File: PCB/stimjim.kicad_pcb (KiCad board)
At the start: 4 copper layers, 129 x 79.5 mm, 224 parts, among them J1 302-R161, J10 USB4105-GF-A, J11 BM03B-SRSS-TB, J2 0731375003, J3 0731375003, J4 10129383-910002ALF, J7 0731375003, J9 0731375003, SW2 PTS645VH58-2 LFS, SW3 TS04-66-50-BK-160-SMT, U1 OPA197, U10 AMP03, U11 INA826, U12 DG409DYZ-T, U13 CC3-0512DF-E, U14 ISO7760, U15 ISO7741, U151 AP2112K-3.3, U16 MC78L05ACDR2G, U17 AD5752, U18 AD7321, U19 AD1582, U2 CC3-0512DF-E, U20 OPA197, U21 AMP03, U22 INA826, U23 DG409DYZ-T, U24 RP2354B, U25 W25Q128JVS, U26 OPA197, U3 ISO7760, U4 ISO7741, U5 MC78L05ACDR2G, U6 AD5752, U7 AD7321, U8 AD1582, U9 OPA197, Y1 ABM8AIG-12.000MHZ-12-2Z-T3

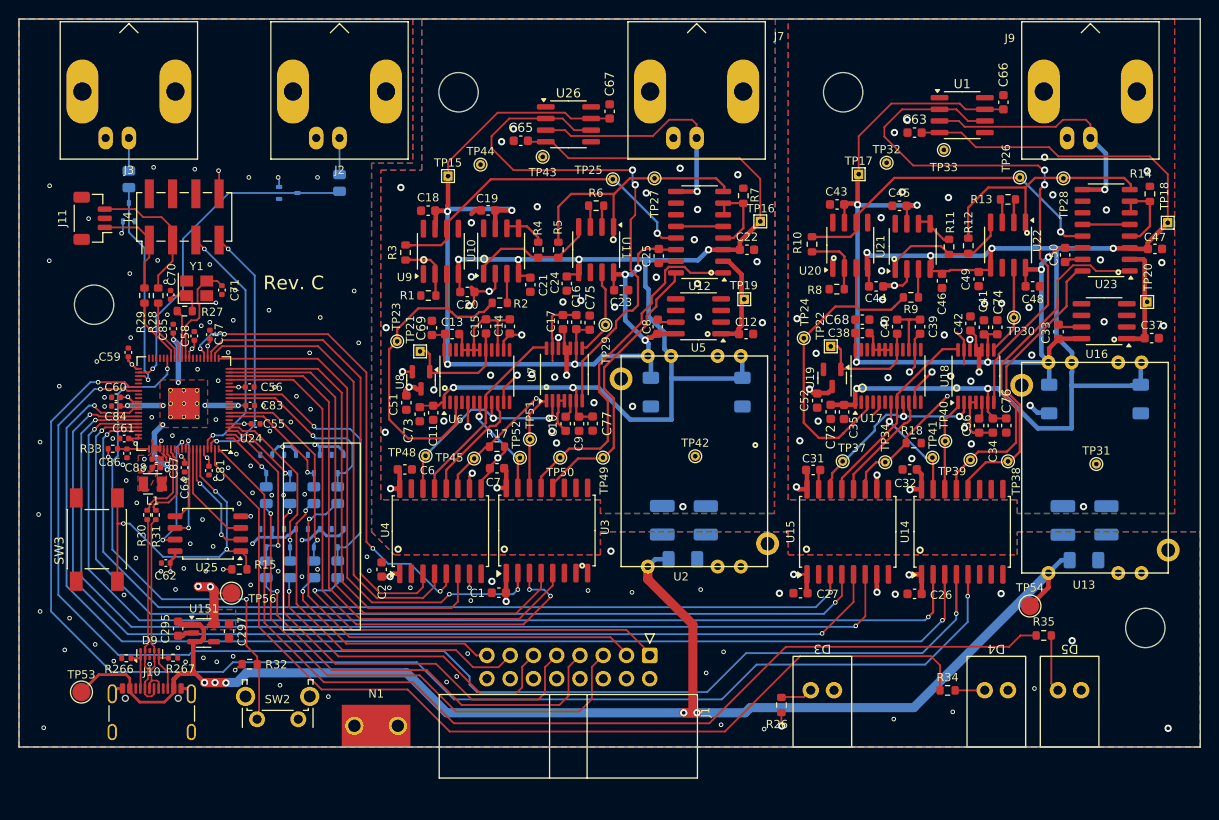
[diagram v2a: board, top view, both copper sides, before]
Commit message: Replace amplifiers
- INA826 -> AD8421
- AMP03 -> LT1995 w/ op-amp in feedback circuit
- Also:
  - update to kicad v10
  - utilize multi-channel layout feature
  - update calculations on schematic
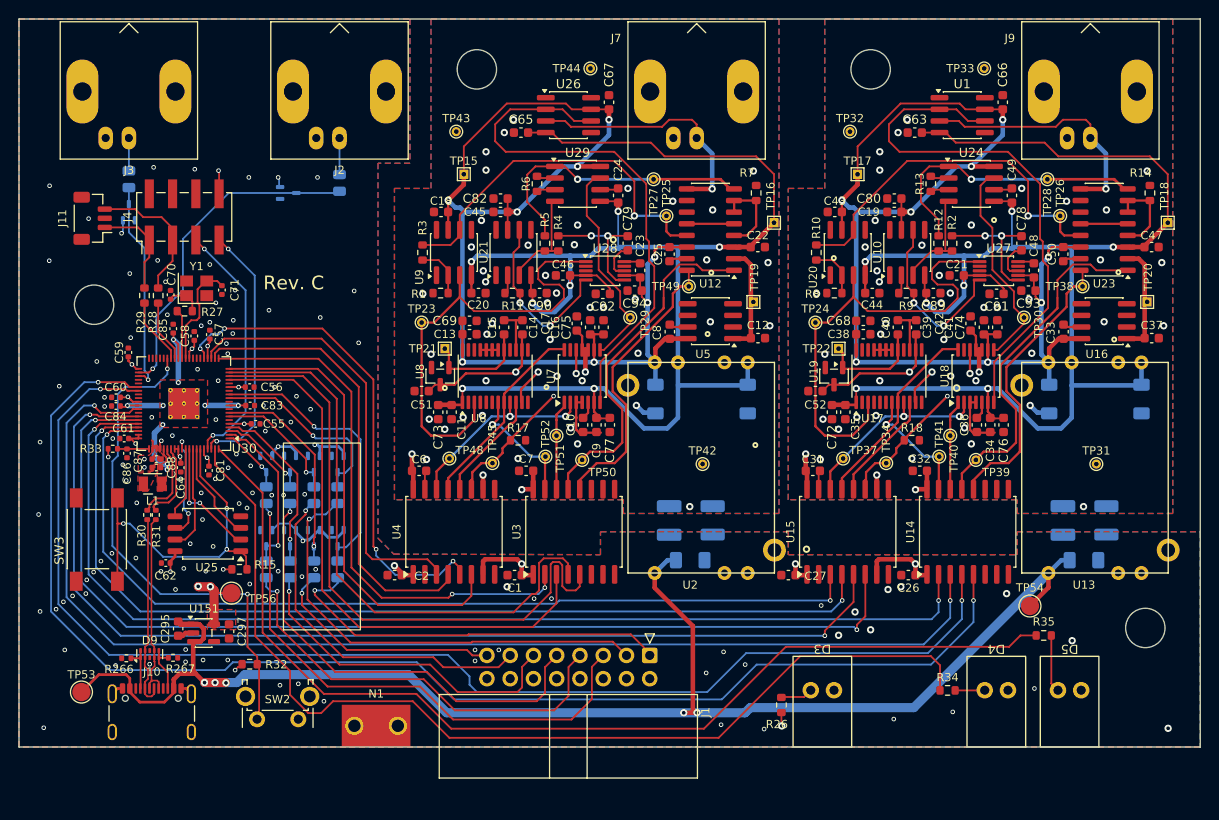
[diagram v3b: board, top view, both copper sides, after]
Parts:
- removed U11, U22: INA826, Package_SO:SOIC-8_3.9x4.9mm_P1.27mm
- added C78: 10p, Capacitor_SMD:C_0603_1608Metric, F.Cu at (256.5, 113.0)
- added C79: 10p, Capacitor_SMD:C_0603_1608Metric, F.Cu at (213.5, 113.0)
- added C80: 0.1uF, Capacitor_SMD:C_0603_1608Metric, F.Cu at (242.6, 108.1)
- added C82: 0.1uF, Capacitor_SMD:C_0603_1608Metric, F.Cu at (199.6, 108.1)
- added C89: 0.1uF, Capacitor_SMD:C_0603_1608Metric, F.Cu at (246.8, 118.4)
- added C90: 0.1uF, Capacitor_SMD:C_0603_1608Metric, F.Cu at (203.8, 118.4)
- added C91: 4.7u, Capacitor_SMD:C_0603_1608Metric, F.Cu at (253.8, 118.5)
- added C92: 4.7u, Capacitor_SMD:C_0603_1608Metric, F.Cu at (210.8, 118.5)
- added C93: 4.7u, Capacitor_SMD:C_0603_1608Metric, F.Cu at (257.2, 118.2)
- added C94: 4.7u, Capacitor_SMD:C_0603_1608Metric, F.Cu at (214.2, 118.2)
- added U27: LT1995, Package_SO:MSOP-10_3x3mm_P0.5mm, F.Cu at (254.0, 116.0)
- added U28: LT1995, Package_SO:MSOP-10_3x3mm_P0.5mm, F.Cu at (211.0, 116.0)
- added U29: AD8421BRZ, Package_SO:SOIC-8_3.9x4.9mm_P1.27mm, F.Cu at (208.0, 106.5)
- added U30: RP2354B, Package_DFN_QFN:QFN-80-1EP_10x10mm_P0.4mm_EP3.4x3.4mm_ThermalVias, F.Cu at (165.0, 130.5)
- C19, C21, C45, C46: value 0.1uF -> 0.01uF
- R11, R9: value 3k -> 1k
- U10, U21: value AMP03 -> OPA197
- U24: value RP2354B -> AD8421BRZ; footprint Package_DFN_QFN:QFN-80-1EP_10x10mm_P0.4mm_EP3.4x3.4mm_ThermalVias -> Package_SO:SOIC-8_3.9x4.9mm_P1.27mm
- moved U24 89.3 mm to (251.0, 106.5), turned to 0 degrees
- moved R2 49.8 mm to (248.9, 113.0), turned to -90 degrees
- moved R11 47.9 mm to (200.9, 118.4), turned to 180 degrees
- moved C21 46.6 mm to (249.4, 116.5), turned to 180 degrees
- moved C19 44.4 mm to (242.6, 109.6)
- moved U10 44.4 mm to (244.0, 114.0)
- moved U21 43.6 mm to (201.0, 114.0)
- moved C45 43.6 mm to (199.6, 109.6)
- moved C46 41.4 mm to (206.4, 116.5), turned to 180 degrees
- moved TP49 20.9 mm to (220.1, 117.7)
- moved TP38 20.8 mm to (263.1, 117.7)
- moved TP44 15.9 mm to (209.4, 93.9)
- moved C24 11.1 mm to (212.4, 107.8), turned to -90 degrees
- moved TP33 9.93 mm to (252.4, 93.9)
- moved TP43 9.83 mm to (194.8, 100.8)
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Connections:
- C19 pad 1: /channel_1/GRND -> /channel_0/GRND
- C19 pad 2: /channel_1/+15V -> /channel_0/+15V
- C21 pad 1: /channel_1/-15V -> /channel_0/-15V
- C21 pad 2: /channel_1/GRND -> /channel_0/GRND
- C45 pad 1: /channel_0/GRND -> /channel_1/GRND
- C45 pad 2: /channel_0/+15V -> /channel_1/+15V
- C46 pad 1: /channel_0/-15V -> /channel_1/-15V
- C46 pad 2: /channel_0/GRND -> /channel_1/GRND
- C71 pad 2: Net-(U24-XIN) -> Net-(U30-XIN)
- C86 pad 1: Net-(U24-VREG_AVDD) -> Net-(U30-VREG_AVDD)
- L1 pad 2: Net-(U24-VREG_LX) -> Net-(U30-VREG_LX)
- R11 pad 1: Net-(U21-REF) -> Net-(U28-REF)
- R11 pad 2: Net-(U21-SENSE) -> Net-(U21--)
- R12 pad 1: Net-(U21-REF) -> Net-(U10-+)
- R13 pad 1: Net-(U22-RG2) -> Net-(R13-Pad1)
- R13 pad 2: Net-(U22-RG) -> Net-(R13-Pad2)
- R2 pad 1: Net-(U10-+) -> /channel_0/HOWLAND_OUTPUT
- R2 pad 2: /channel_1/DAC_OUT -> Net-(U10-+)
- R27 pad 1: Net-(U24-XOUT) -> Net-(U30-XOUT)
- R28 pad 2: Net-(U24-SWCLK) -> Net-(U30-SWCLK)
- R29 pad 2: Net-(U24-SWDIO) -> Net-(U30-SWDIO)
- R32 pad 2: Net-(U24-RUN) -> Net-(U30-RUN)
- R33 pad 2: Net-(U24-VREG_AVDD) -> Net-(U30-VREG_AVDD)
- R34 pad 2: Net-(U24-GPIO2) -> Net-(U30-GPIO2)
- R35 pad 2: Net-(U24-GPIO3) -> Net-(U30-GPIO3)
- R4 pad 1: Net-(U10-REF) -> /channel_1/HOWLAND_OUTPUT
- R4 pad 2: Net-(U10-SENSE) -> Net-(U21-+)
- R5 pad 1: Net-(U10-REF) -> Net-(U21-+)
- R9 pad 1: Net-(U21-+) -> Net-(U27-REF)
- R9 pad 2: /channel_0/DAC_OUT -> Net-(U10--)
- SW2 pad 2: Net-(U24-RUN) -> Net-(U30-RUN)
- U10 pad 1: Net-(U10-REF) -> (no net)
- U10 pad 2: /channel_1/GRND -> Net-(U10--)
- U10 pad 4: /channel_1/-15V -> /channel_0/-15V
- U10 pad 5: Net-(U10-SENSE) -> (no net)
- U10 pad 6: Net-(U10-SENSE) -> Net-(U27-REF)
- U10 pad 7: /channel_1/+15V -> /channel_0/+15V
- U10 pad 8: unconnected-(U10-Pad8) -> (no net)
- U21 pad 1: Net-(U21-REF) -> (no net)
- U21 pad 2: /channel_0/GRND -> Net-(U21--)
- U21 pad 4: /channel_0/-15V -> /channel_1/-15V
- U21 pad 5: Net-(U21-SENSE) -> (no net)
- U21 pad 6: Net-(U21-SENSE) -> Net-(U28-REF)
- U21 pad 7: /channel_0/+15V -> /channel_1/+15V
- U21 pad 8: unconnected-(U21-Pad8) -> (no net)
- U24 pad 1: /MCU/GPIO5 -> /channel_0/I_OUT
- U24 pad 2: /MCU/GPIO4 -> Net-(R13-Pad2)
- U24 pad 3: /MCU/GPIO3 -> Net-(R13-Pad1)
- U24 pad 4: /MCU/GPIO2 -> Net-(U10-+)
- U24 pad 5: VCC -> /channel_0/-15V
- U24 pad 6: unconnected-(U24-GPIO8-Pad6) -> /channel_0/GRND
- U24 pad 7: /MCU/GPIO1 -> /channel_0/I_SENSE
- U24 pad 8: /MCU/GPIO0 -> /channel_0/+15V
- Y1 pad 3: Net-(U24-XIN) -> Net-(U30-XIN)
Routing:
- net Net-(U30-GPIO3): track 0.00 -> 115.1 mm
- net Net-(U24-GPIO3): track 113.8 -> 0.00 mm
- net Net-(U30-GPIO2): track 0.00 -> 111.1 mm
- net Net-(U24-GPIO2): track 107.1 -> 0.00 mm
- net Net-(U30-RUN): track 0.00 -> 56.1 mm, vias 0 -> 2
- net Net-(U24-RUN): track 55.9 -> 0.00 mm, vias 2 -> 0
- net /channel_0/+15V: track 115.2 -> 136.7 mm, vias 6 -> 8
- net /channel_1/-15V: track 141.4 -> 162.9 mm, vias 6 -> 7
- net /channel_1/GRND: track 47.5 -> 27.0 mm, vias 36 -> 44
- net /channel_1/+15V: track 116.1 -> 136.7 mm, vias 7 -> 8
- net Net-(U28-REF): track 0.00 -> 19.9 mm, vias 0 -> 2
- net Net-(U27-REF): track 0.00 -> 19.9 mm, vias 0 -> 2
- net /channel_0/DAC_OUT: track 36.0 -> 51.3 mm
- net Net-(U21-REF): track 15.0 -> 0.00 mm
- net Net-(U10-REF): track 14.8 -> 0.00 mm
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- added copper zone on F.Cu, net Net-(U30-VREG_LX)
- removed copper zone on F.Cu, net Net-(U24-VREG_LX)
